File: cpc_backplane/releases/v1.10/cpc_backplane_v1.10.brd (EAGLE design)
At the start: 99.6 x 81.3 mm, 9 parts

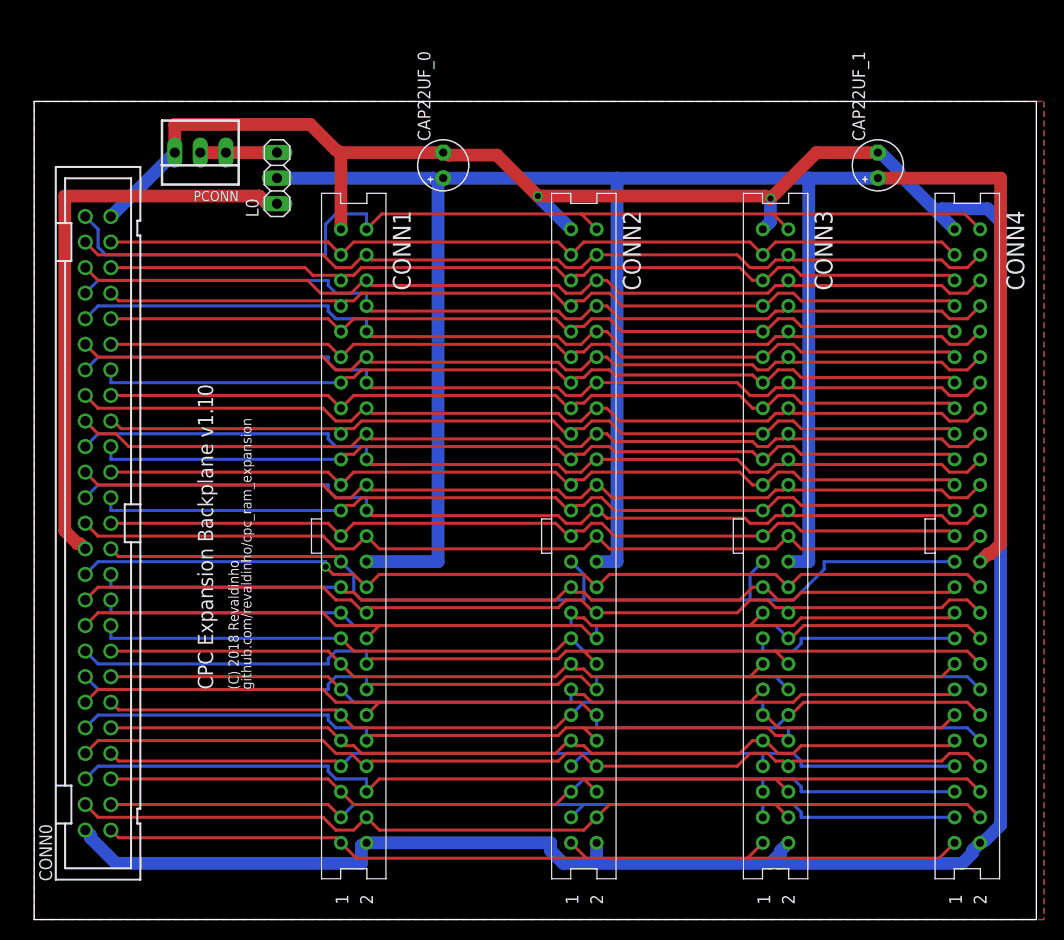
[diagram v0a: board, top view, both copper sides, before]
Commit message: Update backplane releases area
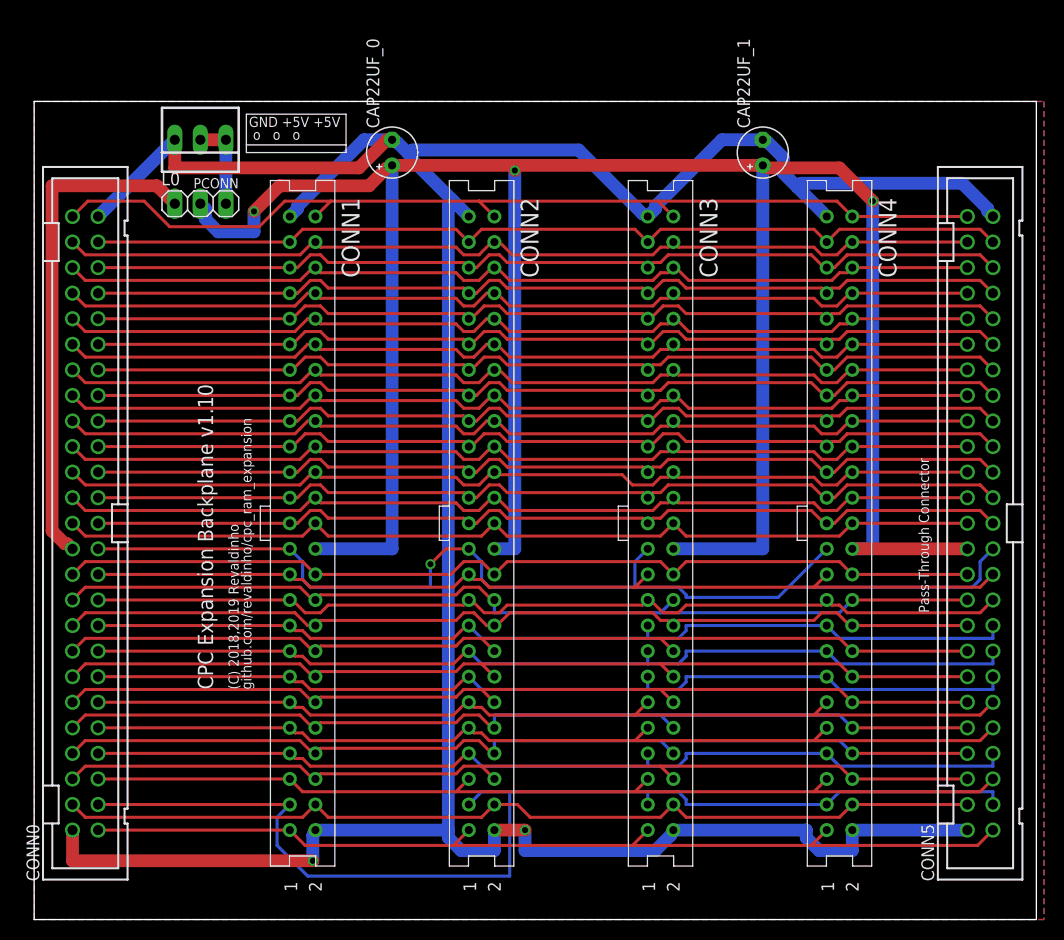
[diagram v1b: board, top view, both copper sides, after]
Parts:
- added CONN5: (no value), con-3m:PAK100/2500-50
- moved CONN4 12.8 mm to (80.0, 39.4)
- moved CONN3 11.5 mm to (62.2, 39.4)
- moved CAP22UF_1 11.5 mm to (72.4, 76.2)
- moved CONN2 10.2 mm to (44.5, 39.4)
- moved L0 8.03 mm to (16.5, 71.1), turned to 0 degrees
- moved CAP22UF_0 5.24 mm to (35.6, 76.2)
- moved CONN1 5.24 mm to (26.7, 39.4)
- moved CONN0 1.27 mm to (5.08, 39.4)
- moved PCONN 1.27 mm to (16.5, 77.5)
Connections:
- net A0: now also CONN5.33
- net A1: now also CONN5.34
- net A10: now also CONN5.43
- net A11: now also CONN5.44
- net A12: now also CONN5.45
- net A13: now also CONN5.46
- net A14: now also CONN5.47
- net A15: now also CONN5.48
- net A2: now also CONN5.35
- net A3: now also CONN5.36
- net A4: now also CONN5.37
- net A5: now also CONN5.38
- net A6: now also CONN5.39
- net A7: now also CONN5.40
- net A8: now also CONN5.41
- net A9: now also CONN5.42
- net BUSACK_B: now also CONN5.13
- net BUSRESET_B: now also CONN5.11
- net BUSRQ_B: now also CONN5.14
- net CLK: now also CONN5.1
- net CURSOR: now also CONN5.5
- net D0: now also CONN5.25
- net D1: now also CONN5.26
- net D2: now also CONN5.27
- net D3: now also CONN5.28
- net D4: now also CONN5.29
- net D5: now also CONN5.30
- net D6: now also CONN5.31
- net D7: now also CONN5.32
- net EXP_B: now also CONN5.3
- net HALT_B: now also CONN5.17
- net INT_B: now also CONN5.16
- net IOREQ_B: now also CONN5.20
- net LPEN: now also CONN5.4
- net M1_B: now also CONN5.22
- net MREQ_B: now also CONN5.23
- net NMI_B: now also CONN5.15
- net RAMDIS: now also CONN5.6
- net RAMRD_B: now also CONN5.7
- net RD_B: now also CONN5.19
- net READY: now also CONN5.12
- net RESET_B: now also CONN5.10
- net RFSH_B: now also CONN5.21
- net ROMDIS: now also CONN5.8
- net ROMEN_B: now also CONN5.9
- net SOUND: now also CONN5.50
- net VDD1: now also CONN5.24
- net VSS: now also CONN5.2, CONN5.49
- net WR_B: now also CONN5.18
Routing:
- net EXP_B: track 88.8 -> 112.9 mm
- net VSS: track 281.7 -> 300.6 mm
- net VDD1: track 236.3 -> 254.7 mm, vias 0 -> 3
- net MREQ_B: track 98.0 -> 110.4 mm, vias 0 -> 1
- net VDD_CPC: track 57.4 -> 50.0 mm
- net CURSOR: track 88.0 -> 95.3 mm
- net ROMEN_B: track 87.5 -> 94.6 mm
- net CLK: track 89.9 -> 96.6 mm
- net BUSRESET_B: track 88.2 -> 94.6 mm
- net RFSH_B: track 88.2 -> 94.6 mm
- net NMI_B: track 88.2 -> 94.4 mm
- net A12: track 87.5 -> 93.1 mm
- net RAMRD_B: track 88.8 -> 94.4 mm
- net D0: track 87.5 -> 93.1 mm
- net A8: track 87.5 -> 93.1 mm
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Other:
- board text added: "(C) 2018,2019 Revaldinho"
- board text added: "GND +5V +5V"
- board text added: "Pass-Through Connector"
- board text added: "o o o"
- board text removed: "(C) 2018 Revaldinho"
